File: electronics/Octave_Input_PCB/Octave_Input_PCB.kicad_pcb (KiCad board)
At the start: 2 copper layers, 87.8 x 95.8 mm, 57 parts, among them J1 HRO_TYPE-C-31-M-12, SW1 SW_Hot_Swap_Socket, SW10 SW_Hot_Swap_Socket, SW11 SW_Hot_Swap_Socket, SW12 SW_Hot_Swap_Socket, SW13 SW_Hot_Swap_Socket, SW14 Alps_Alpine_RKJXV1224, SW15 Bourns_PEC12R-4xxxF-Sxxx, SW2 SW_Hot_Swap_Socket, SW3 SW_Hot_Swap_Socket, SW4 SW_Hot_Swap_Socket, SW5 SW_Hot_Swap_Socket, SW6 SW_Hot_Swap_Socket, SW7 SW_Hot_Swap_Socket, SW8 SW_Hot_Swap_Socket, SW9 SW_Hot_Swap_Socket, U1 AP2112K-3.3, U2 Raspberry_Pi_RP2040

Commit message: [WIP] Update schematic and PCB
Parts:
- added U3: W25Q64JVSS, Package_SO:SOIC-8_5.23x5.23mm_P1.27mm, F.Cu at (66.7, 104.8)
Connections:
- U2 pad 51: unconnected-(U2-Pad51) -> QSPI_SD3
- U2 pad 52: unconnected-(U2-Pad52) -> QSPI_SCLK
- U2 pad 53: unconnected-(U2-Pad53) -> QSPI_SD0
- U2 pad 54: unconnected-(U2-Pad54) -> QSPI_SD2
- U2 pad 55: unconnected-(U2-Pad55) -> QSPI_SD1
- U2 pad 56: unconnected-(U2-Pad56) -> QSPI_SS_N
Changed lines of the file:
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@@
   (net 76 "unconnected-(U2-Pad40)")
   (net 77 "unconnected-(U2-Pad41)")
-  (net 78 "unconnected-(U2-Pad51)")
-  (net 79 "unconnected-(U2-Pad52)")
-  (net 80 "unconnected-(U2-Pad53)")
-  (net 81 "unconnected-(U2-Pad54)")
-  (net 82 "unconnected-(U2-Pad55)")
-  (net 83 "unconnected-(U2-Pad56)")
+  (net 78 "QSPI_SD3")
+  (net 79 "QSPI_SCLK")
+  (net 80 "QSPI_SD0")
+  (net 81 "QSPI_SD2")
+  (net 82 "QSPI_SD1")
+  (net 83 "QSPI_SS_N")
   (footprint "Octave_Library:R_0805_2012Metric" (layer "F.Cu")
     (at 57.15 126.365 -90)
@@
       (net 38 "+1V1") (pinfunction "DVDD") (pintype "power_in"))
     (pad "51" smd roundrect (at -0.6 -3.4375 90) (size 0.875 0.2) (layers "F.Cu" "F.Paste" "F.Mask") (roundrect_rratio 0.25)
-      (net 78 "unconnected-(U2-Pad51)") (pinfunction "QSPI_SD3") (pintype "bidirectional"))
+      (net 78 "QSPI_SD3") (pinfunction "QSPI_SD3") (pintype "bidirectional"))
     (pad "52" smd roundrect (at -1 -3.4375 90) (size 0.875 0.2) (layers "F.Cu" "F.Paste" "F.Mask") (roundrect_rratio 0.25)
-      (net 79 "unconnected-(U2-Pad52)") (pinfunction "QSPI_SCLK") (pintype "output"))
+      (net 79 "QSPI_SCLK") (pinfunction "QSPI_SCLK") (pintype "output"))
     (pad "53" smd roundrect (at -1.4 -3.4375 90) (size 0.875 0.2) (layers "F.Cu" "F.Paste" "F.Mask") (roundrect_rratio 0.25)
-      (net 80 "unconnected-(U2-Pad53)") (pinfunction "QSPI_SD0") (pintype "bidirectional"))
+      (net 80 "QSPI_SD0") (pinfunction "QSPI_SD0") (pintype "bidirectional"))
     (pad "54" smd roundrect (at -1.8 -3.4375 90) (size 0.875 0.2) (layers "F.Cu" "F.Paste" "F.Mask") (roundrect_rratio 0.25)
-      (net 81 "unconnected-(U2-Pad54)") (pinfunction "QSPI_SD2") (pintype "bidirectional"))
+      (net 81 "QSPI_SD2") (pinfunction "QSPI_SD2") (pintype "bidirectional"))
     (pad "55" smd roundrect (at -2.2 -3.4375 90) (size 0.875 0.2) (layers "F.Cu" "F.Paste" "F.Mask") (roundrect_rratio 0.25)
-      (net 82 "unconnected-(U2-Pad55)") (pinfunction "QSPI_SD1") (pintype "bidirectional"))
+      (net 82 "QSPI_SD1") (pinfunction "QSPI_SD1") (pintype "bidirectional"))
     (pad "56" smd roundrect (at -2.6 -3.4375 90) (size 0.875 0.2) (layers "F.Cu" "F.Paste" "F.Mask") (roundrect_rratio 0.25)
-      (net 83 "unconnected-(U2-Pad56)") (pinfunction "QSPI_SS_N") (pintype "bidirectional"))
+      (net 83 "QSPI_SS_N") (pinfunction "QSPI_SS_N") (pintype "bidirectional"))
     (pad "57" smd roundrect (at 0 0) (size 3.2 3.2) (layers "F.Cu" "F.Paste" "F.Mask") (roundrect_rratio 0.045)
       (net 28 "GND") (pinfunction "GND") (pintype "power_in"))
@@
       (offset (xyz 0 0 0))
       (scale (xyz 1 1 1))
+      (rotate (xyz 0 0 0))
+    )
+  )
+  (footprint "Package_SO:SOIC-8_5.23x5.23mm_P1.27mm" (layer "F.Cu")
+    (at 66.675 104.775)
+    (descr "SOIC, 8 Pin (http://www.winbond.com/resource-files/w25q32jv%20revg%2003272018%20plus.pdf#page=68), generated with kicad-footprint-generator ipc_gullwing_generator.py")
+    (tags "SOIC SO")
+    (property "Sheetfile" "Octave_Input_PCB.kicad_sch")
+    (property "Sheetname" "")
+    (attr smd)
+    (fp_text reference "U3" (at 0 -3.56) (layer "F.SilkS")
+      (effects (font (size 1 1) (thickness 0.15)))
+    )
+    (fp_text value "W25Q64JVSS" (at 0 3.56) (layer "F.Fab")
+      (effects (font (size 1 1) (thickness 0.15)))
+    )
+    (fp_text user "${REFERENCE}" (at 0 0) (layer "F.Fab")
+      (effects (font (size 1 1) (thickness 0.15)))
+    )
+    (fp_line (start 0 2.725) (end -2.725 2.725) (layer "F.SilkS") (width 0.12))
+    (fp_line (start -2.725 -2.725) (end -2.725 -2.465) (layer "F.SilkS") (width 0.12))
+    (fp_line (start -2.725 -2.465) (end -4.4 -2.465) (layer "F.SilkS") (width 0.12))
+    (fp_line (start 0 2.725) (end 2.725 2.725) (layer "F.SilkS") (width 0.12))
+    (fp_line (start 2.725 2.725) (end 2.725 2.465) (layer "F.SilkS") (width 0.12))
+    (fp_line (start -2.725 2.725) (end -2.725 2.465) (layer "F.SilkS") (width 0.12))
+    (fp_line (start 0 -2.725) (end -2.725 -2.725) (layer "F.SilkS") (width 0.12))
+    (fp_line (start 2.725 -2.725) (end 2.725 -2.465) (layer "F.SilkS") (width 0.12))
+    (fp_line (start 0 -2.725) (end 2.725 -2.725) (layer "F.SilkS") (width 0.12))
+    (fp_line (start 4.65 -2.86) (end -4.65 -2.86) (layer "F.CrtYd") (width 0.05))
+    (fp_line (start -4.65 -2.86) (end -4.65 2.86) (layer "F.CrtYd") (width 0.05))
+    (fp_line (start -4.65 2.86) (end 4.65 2.86) (layer "F.CrtYd") (width 0.05))
+    (fp_line (start 4.65 2.86) (end 4.65 -2.86) (layer "F.CrtYd") (width 0.05))
+    (fp_line (start -1.615 -2.615) (end 2.615 -2.615) (layer "F.Fab") (width 0.1))
+    (fp_line (start -2.615 2.615) (end -2.615 -1.615) (layer "F.Fab") (width 0.1))
+    (fp_line (start 2.615 -2.615) (end 2.615 2.615) (layer "F.Fab") (width 0.1))
+    (fp_line (start 2.615 2.615) (end -2.615 2.615) (layer "F.Fab") (width 0.1))
+    (fp_line (start -2.615 -1.615) (end -1.615 -2.615) (layer "F.Fab") (width 0.1))
+    (pad "1" smd roundrect (at -3.6 -1.905) (size 1.6 0.6) (layers "F.Cu" "F.Paste" "F.Mask") (roundrect_rratio 0.25)
+      (net 83 "QSPI_SS_N") (pinfunction "~{CS}") (pintype "input"))
+    (pad "2" smd roundrect (at -3.6 -0.635) (size 1.6 0.6) (layers "F.Cu" "F.Paste" "F.Mask") (roundrect_rratio 0.25)
+      (net 82 "QSPI_SD1") (pinfunction "DO(IO1)") (pintype "bidirectional"))
+    (pad "3" smd roundrect (at -3.6 0.635) (size 1.6 0.6) (layers "F.Cu" "F.Paste" "F.Mask") (roundrect_rratio 0.25)
+      (net 81 "QSPI_SD2") (pinfunction "IO2") (pintype "bidirectional"))
+    (pad "4" smd roundrect (at -3.6 1.905) (size 1.6 0.6) (layers "F.Cu" "F.Paste" "F.Mask") (roundrect_rratio 0.25)
+      (net 28 "GND") (pinfunction "GND") (pintype "power_in"))
+    (pad "5" smd roundrect (at 3.6 1.905) (size 1.6 0.6) (layers "F.Cu" "F.Paste" "F.Mask") (roundrect_rratio 0.25)
+      (net 80 "QSPI_SD0") (pinfunction "DI(IO0)") (pintype "bidirectional"))
+    (pad "6" smd roundrect (at 3.6 0.635) (size 1.6 0.6) (layers "F.Cu" "F.Paste" "F.Mask") (roundrect_rratio 0.25)
+      (net 79 "QSPI_SCLK") (pinfunction "CLK") (pintype "input"))
+    (pad "7" smd roundrect (at 3.6 -0.635) (size 1.6 0.6) (layers "F.Cu" "F.Paste" "F.Mask") (roundrect_rratio 0.25)
+      (net 78 "QSPI_SD3") (pinfunction "IO3") (pintype "bidirectional"))
+    (pad "8" smd roundrect (at 3.6 -1.905) (size 1.6 0.6) (layers "F.Cu" "F.Paste" "F.Mask") (roundrect_rratio 0.25)
+      (net 24 "+3V3") (pinfunction "VCC") (pintype "power_in"))
+    (model "${KICAD6_3DMODEL_DIR}/Package_SO.3dshapes/SOIC-8_5.23x5.23mm_P1.27mm.wrl"
+      (offset (xyz 0 0 0))
+      (scale (xyz 1 1 1))

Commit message: [WIP] Update PCB
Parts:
- moved C2 2.51 mm to (82.8, 64.4)
- moved U1 2.38 mm to (82.3, 61.9)
- moved C1 2.20 mm to (82.8, 59.4)
- moved C3 0.75 mm to (89.9, 99.1)
- moved C4 0.75 mm to (88.9, 99.1)
- moved C5 0.40 mm to (80.1, 102.0)
- moved C9 0.40 mm to (91.4, 102.0)
- moved C6 0.40 mm to (80.1, 106.0)
- moved C8 0.40 mm to (91.4, 106.0)
- moved C14 0.39 mm to (91.4, 101.0)
- moved C10 0.22 mm to (84.9, 97.7)
- moved C12 0.22 mm to (83.9, 97.7)
- moved C13 0.22 mm to (85.9, 97.7)
- moved R3 0.20 mm to (86.9, 98.4)
- moved R4 0.20 mm to (87.9, 98.4)
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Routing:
- net row1: track 108.6 -> 51.4 mm
- net row0: track 129.2 -> 72.1 mm
- net row2: track 63.1 -> 5.96 mm
- net Net-(J1-PadA6): track 3.17 -> 50.0 mm
- net Net-(J1-PadA7): track 3.17 -> 48.7 mm
- net GND: track 0.00 -> 36.3 mm, vias 0 -> 6
- net +3V3: track 8.24 -> 44.5 mm
- net QSPI_SD3: track 0.00 -> 22.2 mm
- net QSPI_SCLK: track 0.00 -> 20.0 mm
- net QSPI_SD0: track 0.00 -> 17.9 mm
- net +5V: track 7.40 -> 23.6 mm, vias 0 -> 2
- net +1V1: track 1.50 -> 13.3 mm
- net QSPI_SD2: track 0.00 -> 4.73 mm
- net QSPI_SD1: track 0.00 -> 4.15 mm
- net QSPI_SS_N: track 0.00 -> 2.89 mm
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
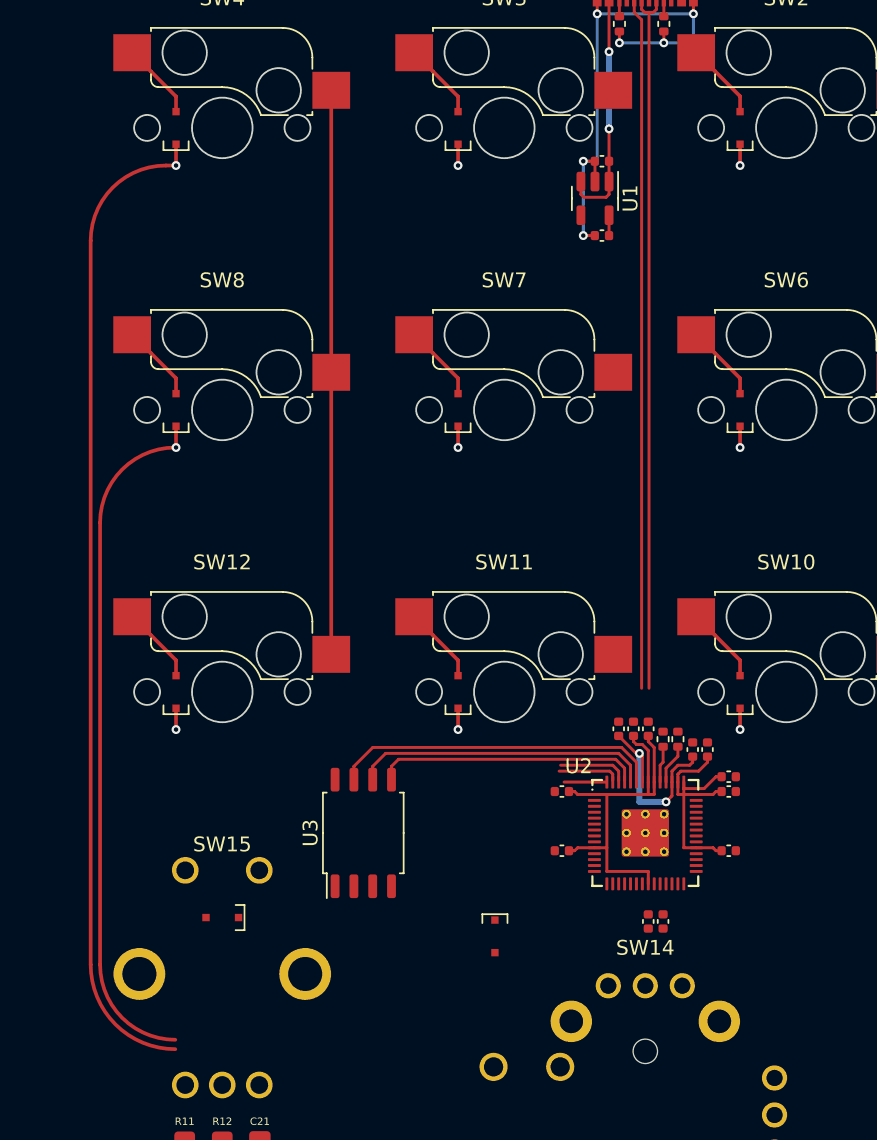
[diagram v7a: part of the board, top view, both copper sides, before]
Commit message: Add crystal resonator
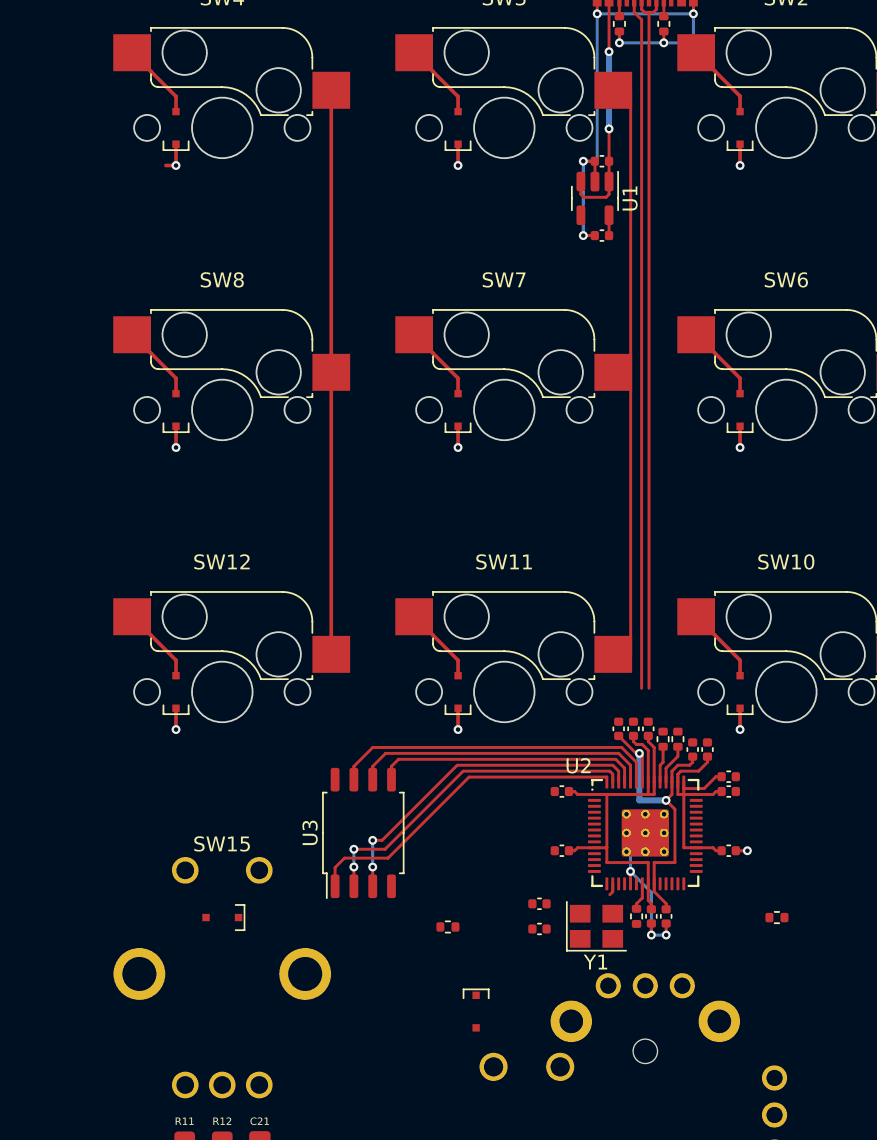
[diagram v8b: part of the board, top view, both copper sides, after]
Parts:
- added C15: 30pF, Capacitor_SMD:C_0402_1005Metric, F.Cu at (78.6, 109.6)
- added C16: 30pF, Capacitor_SMD:C_0402_1005Metric, F.Cu at (78.6, 111.3)
- added R5: 10K, Resistor_SMD:R_0402_1005Metric, F.Cu at (94.6, 110.5)
- added R6: 1K, Resistor_SMD:R_0402_1005Metric, F.Cu at (72.4, 111.1)
- added R7: 1K, Resistor_SMD:R_0402_1005Metric, F.Cu at (85.1, 110.4)
- added Y1: 12MHz, Crystal:Crystal_SMD_3225-4Pin_3.2x2.5mm, F.Cu at (82.4, 111.1)
- moved D14 5.24 mm to (74.3, 116.8)
- moved C11 0.40 mm to (87.1, 110.4)
- moved C7 0.40 mm to (86.1, 110.4)
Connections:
- U2 pad 20: unconnected-(U2-Pad20) -> Net-(U2-Pad20)
- U2 pad 21: unconnected-(U2-Pad21) -> Net-(U2-Pad21)
- U2 pad 26: unconnected-(U2-Pad26) -> ~{RESET}
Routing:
- net row0: track 72.1 -> 6.65 mm
- net row1: track 51.4 -> 6.01 mm
- net col2: track 0.00 -> 38.1 mm
- net QSPI_SS_N: track 2.89 -> 22.2 mm
- net QSPI_SD1: track 4.15 -> 22.8 mm, vias 0 -> 2
- net QSPI_SD2: track 4.73 -> 22.7 mm, vias 0 -> 2
- net GND: track 36.3 -> 46.8 mm, vias 6 -> 10
- net +1V1: track 13.3 -> 22.4 mm
- net Net-(U2-Pad21): track 0.00 -> 1.88 mm
- net +3V3: track 44.5 -> 46.3 mm
- net unconnected-(U2-Pad16): track 0.00 -> 0.82 mm
